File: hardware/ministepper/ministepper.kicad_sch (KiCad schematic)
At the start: 13 parts, among them J2 Conn_ARM_SWD_TagConnect_TC203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, U1 STM32G071G8U6, U4 SIT3088EEUA

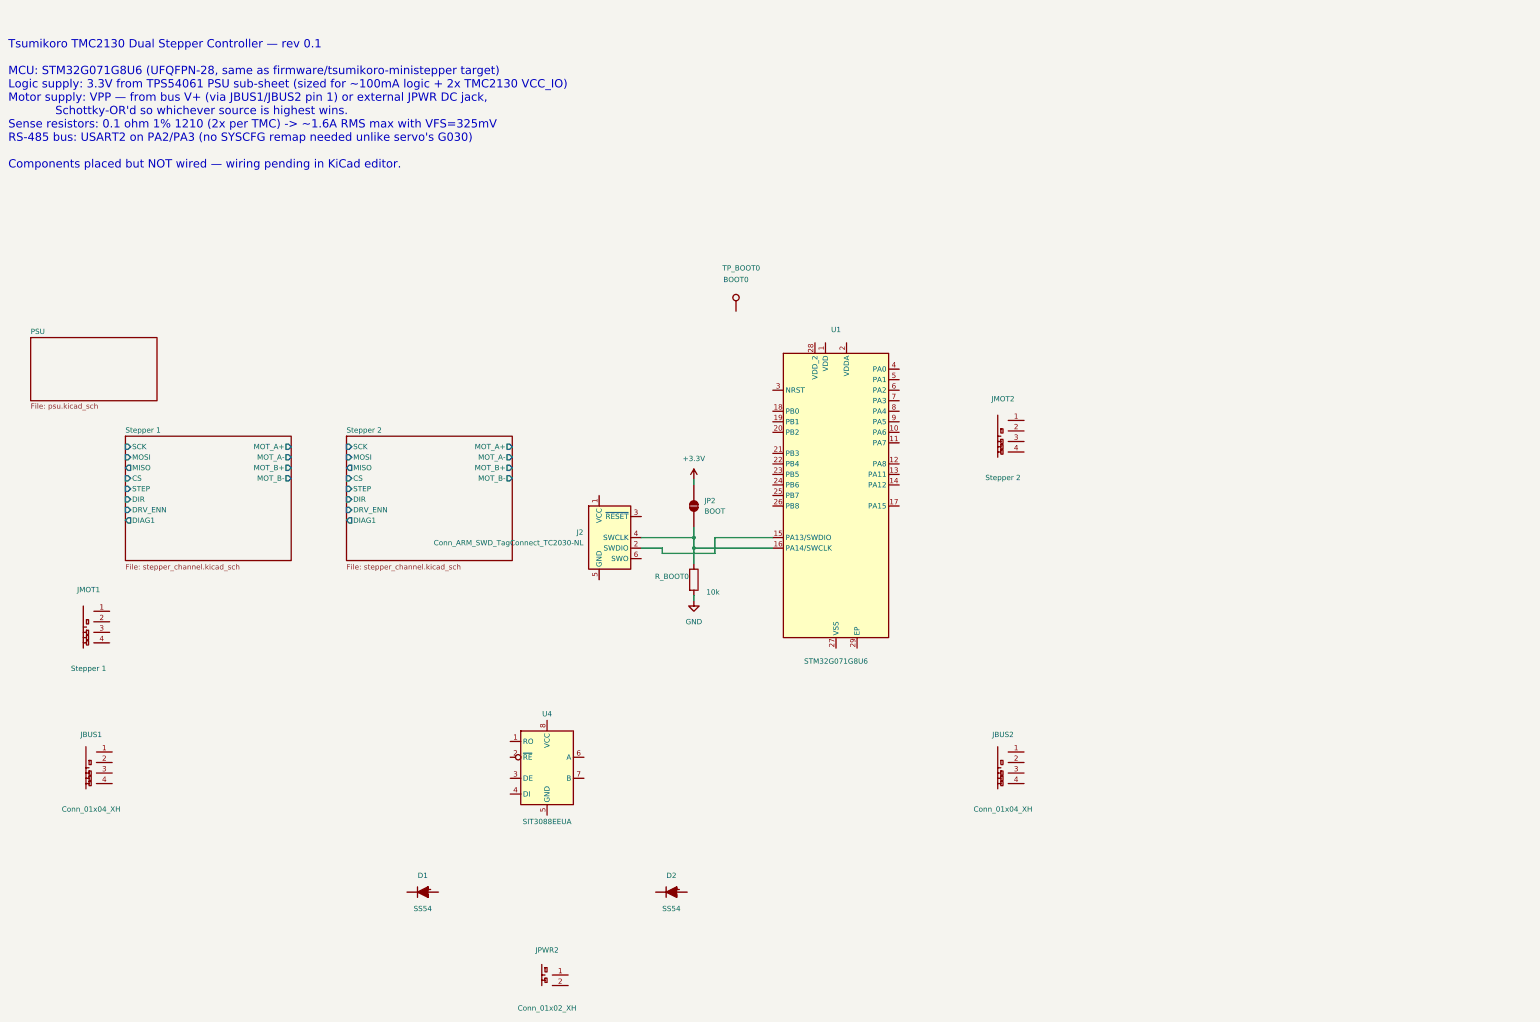
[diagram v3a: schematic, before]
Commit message: hw+fw: fix STM32G071G8U6 UFQFPN28 symbol + pin map
The tsumikoro:STM32G071G8U6 symbol had a fabricated pin map that
didn't match ST DS12232 Figure 9 — VDD/VDDA were split onto pins 1/2
(they're actually fused on pin 3 on this package), NRST was assigned
to pin 3 (it's on pin 5), pin 28 was labelled VDD_2 (it's PB8), and
DIR2 was on PB2 (which is not bonded out on UFQFPN28).

Because the ministepper is not yet wired and firmware addresses GPIOs
by port name, no PCB damage resulted — but every pin number in docs,
firmware comments, and the symbol was off.

Rewritten against the datasheet:

- Symbol rebuilt with the real 29-pin UFQFPN28 layout (28 signal +
  EP), including PC14/PC15 on pins 1/2 and PC6 on pin 17.
- DIR2 reassigned from phantom PB2 to PC6 (pin 17).
- GPIOC clock enabled in firmware for PC6.
- CLAUDE.md and ministepper/docs/README.md pin tables rewritten.
- docs/README now calls out required MCU decoupling (100 nF + 4.7 µF
  bulk + NRST filter) that was implicitly missing when docs assumed
  two separate VDD pins.

Co-Authored-By: Claude Opus 4.6 (1M context) <noreply@anthropic.com>
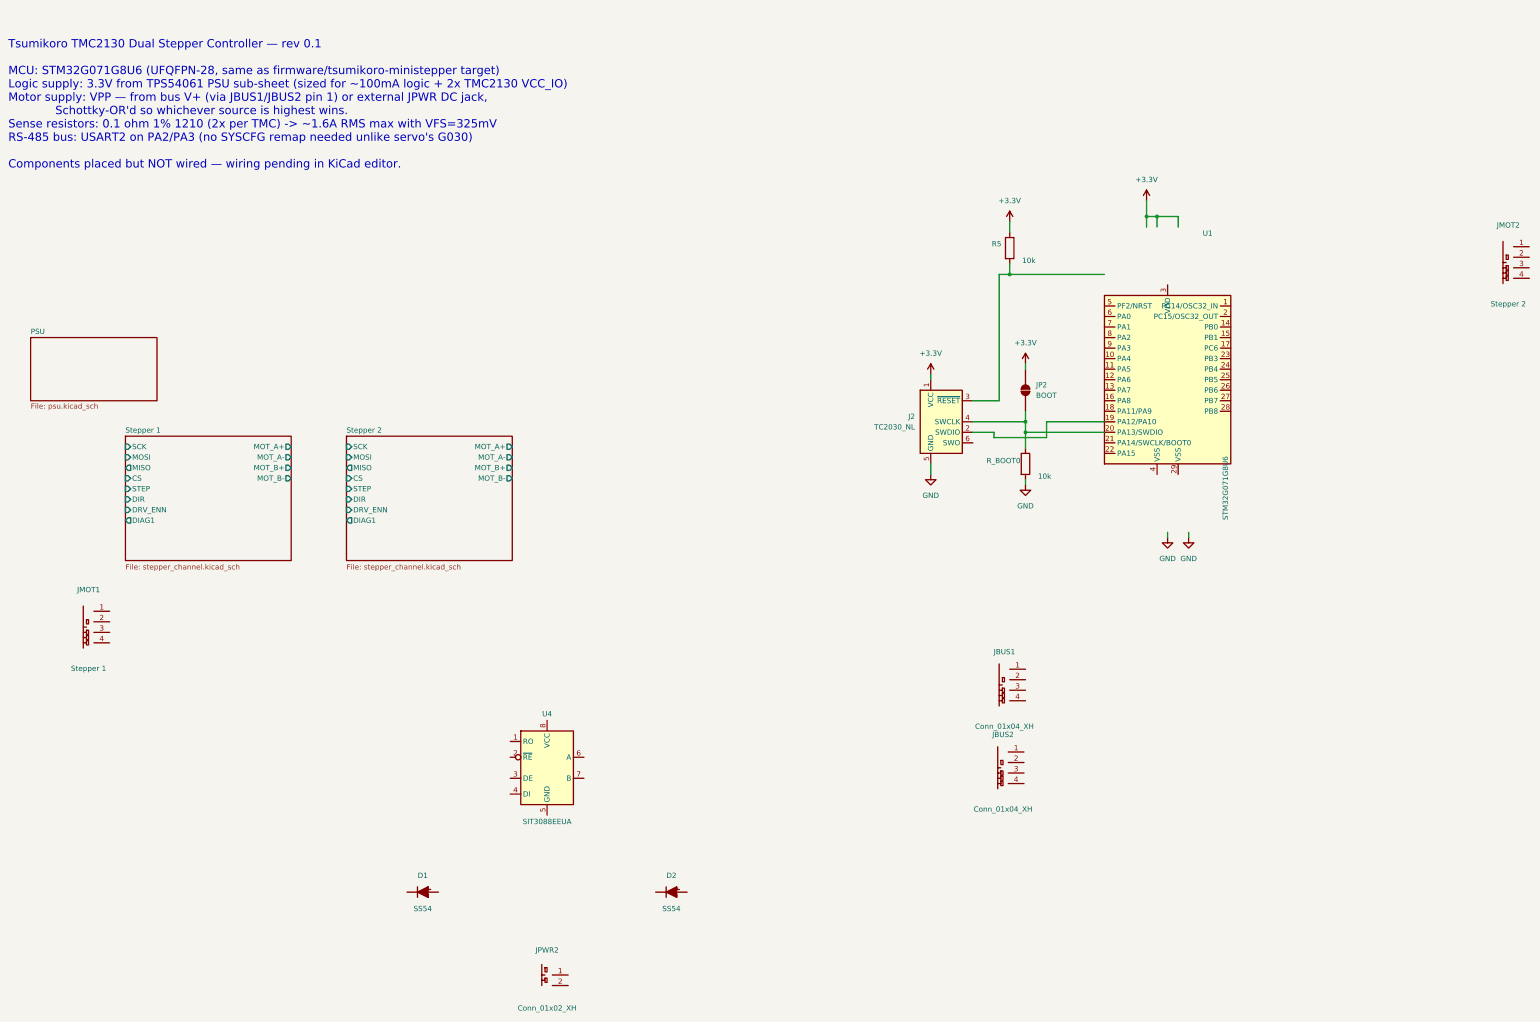
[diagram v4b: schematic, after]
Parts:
- removed TP_BOOT0: BOOT0, TestPoint:TestPoint_Pad_1.0x1.0mm, symbol Connector:TestPoint
- added R5: 10k, Resistor_SMD:R_0402_1005Metric, symbol Device:R
- J2: value Conn_ARM_SWD_TagConnect_TC2030-NL -> TC2030_NL
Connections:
- net +3.3V: now also J2.1 (VCC), R5.1
- net GND: now also J2.5 (GND)
- net at J2.2 (SWDIO): now also U1.19 (PA12/PA10); no longer U1.15 (PA13/SWDIO)
- net at J2.3 (~{RESET}): now also R5.2
- net at J2.4 (SWCLK), JP2.1 (A), R_BOOT0.1: now also U1.20 (PA13/SWDIO); no longer U1.16 (PA14/SWCLK)
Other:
- moved on the sheet: J2, JBUS1, JMOT2, JP2, R_BOOT0, U1

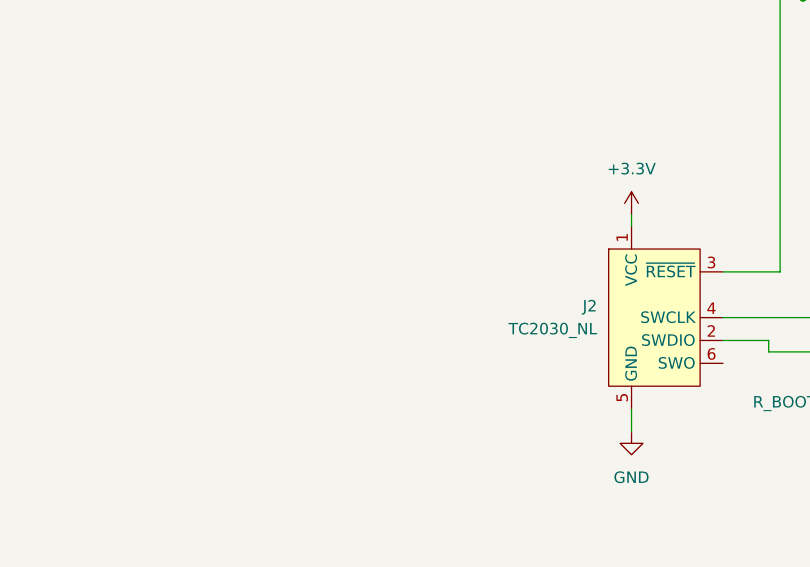
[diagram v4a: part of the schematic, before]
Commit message: hw/ministepper: add MCU decoupling + NRST filter caps
Rev 0.1 root schematic had zero MCU support caps on the STM32G071 —
all existing caps were PSU sub-sheet or TMC2130 sub-sheet parts. Per
ST AN2867 / G071 datasheet hardware design recommendations:

- C_MCU_VDD (100 nF 0402 C307331, basic) — VDD/VDDA HF bypass at pin 3.
- C_MCU_BULK (4.7 uF 0603 C19666 Samsung, basic) — bulk decoupling
  close to the VDD pin.
- C_NRST (100 nF 0402 C307331, basic) — noise filter on NRST pin 5.

Also embedded Device:C in the root schematic's lib_symbols block.
Without that embedding, any root-level capacitor would silently fail
BOM export — KiCad drops symbols whose lib_id isn't cached in the
schematic. Only Device:R had been embedded previously.

Co-Authored-By: Claude Opus 4.6 (1M context) <noreply@anthropic.com>
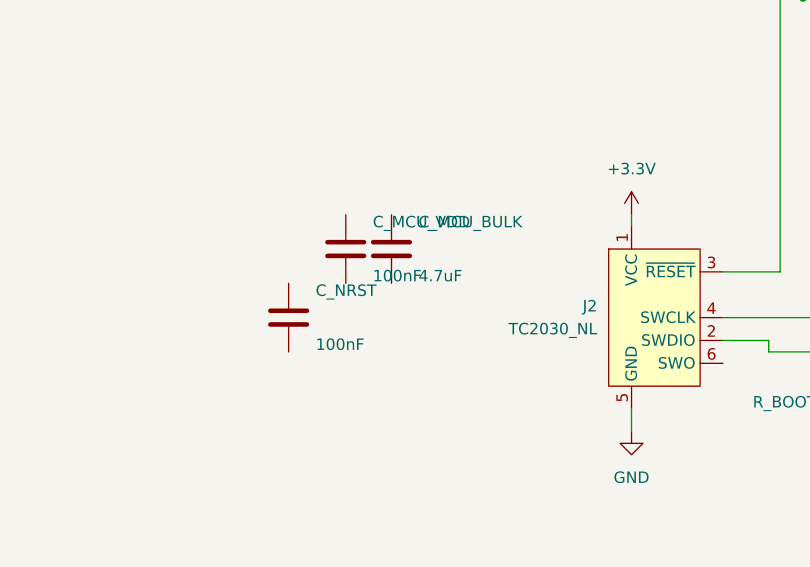
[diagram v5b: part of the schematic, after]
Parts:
- added C_MCU_BULK: 4.7uF, Capacitor_SMD:C_0603_1608Metric, symbol Device:C
- added C_MCU_VDD, C_NRST: 100nF, Capacitor_SMD:C_0402_1005Metric, symbol Device:C

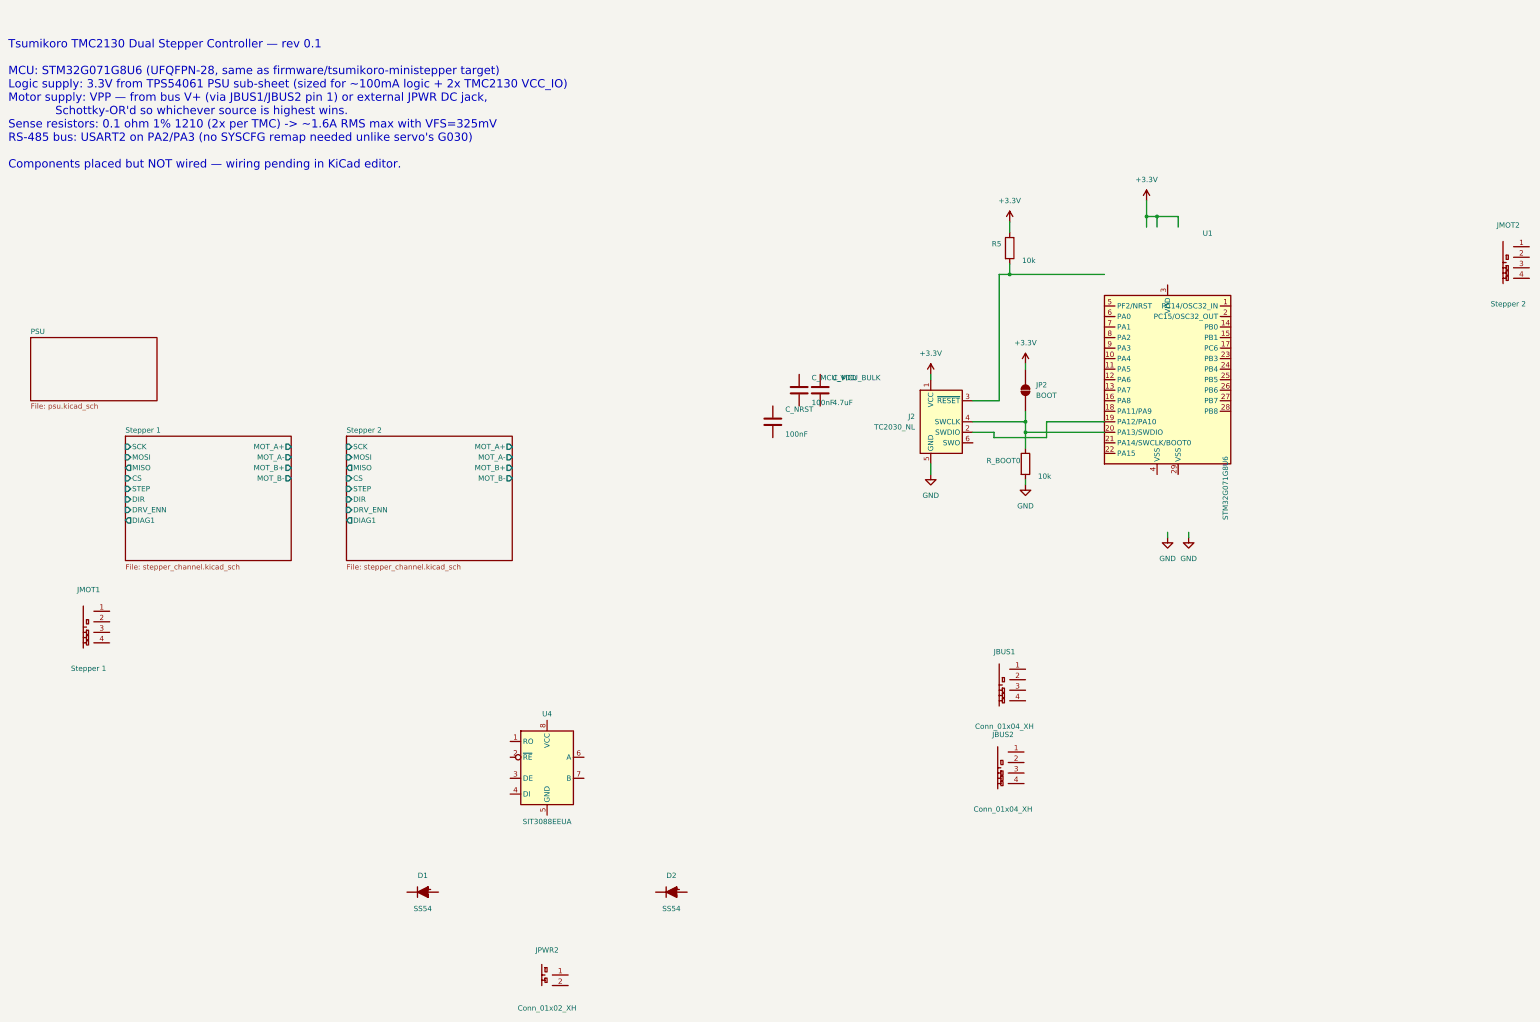
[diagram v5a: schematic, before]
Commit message: hw/ministepper: swap MCU to STM32G0B1KBU6 (USB) + add USB-C connector
Replace the STM32G071G8U6 (UFQFPN-28, no USB) with STM32G0B1KBU6
(UFQFPN-32, USB 2.0 FS, 128KB flash, 144KB RAM). This frees PA11/PA12
for USB D−/D+ by giving PA9/PA10 as separate pins.

Hardware changes:
- New UFQFPN-32 5x5mm footprint + STEP model (from EasyEDA C5159549)
- New tsumikoro:STM32G0B1KBU6 symbol with 32-pin + EP layout
- J_USB: GCT USB4105-xx-A 16-pin USB-C receptacle (C2927039, same as
  bridge board) with R_CC1/R_CC2 5.1k pull-downs for device/sink
- DRV_ENN moved PA11 → PB2 (pin 17)
- TMC2_CS moved PA12 → PA9 (pin 19)
- PA11 (pin 22) = USB D−, PA12 (pin 23) = USB D+
- No external crystal needed (HSI48 + CRS from USB SOF)

Firmware:
- PIN_DRV_ENN: GPIOA/11 → GPIOB/2
- PIN_TMC2_CS: GPIOA/12 → GPIOA/9
- Target header updated to rev 0.2 / UFQFPN-32

Docs: CLAUDE.md and ministepper/docs/README.md pin maps rewritten
for the 32-pin layout.

Co-Authored-By: Claude Opus 4.6 (1M context) <noreply@anthropic.com>
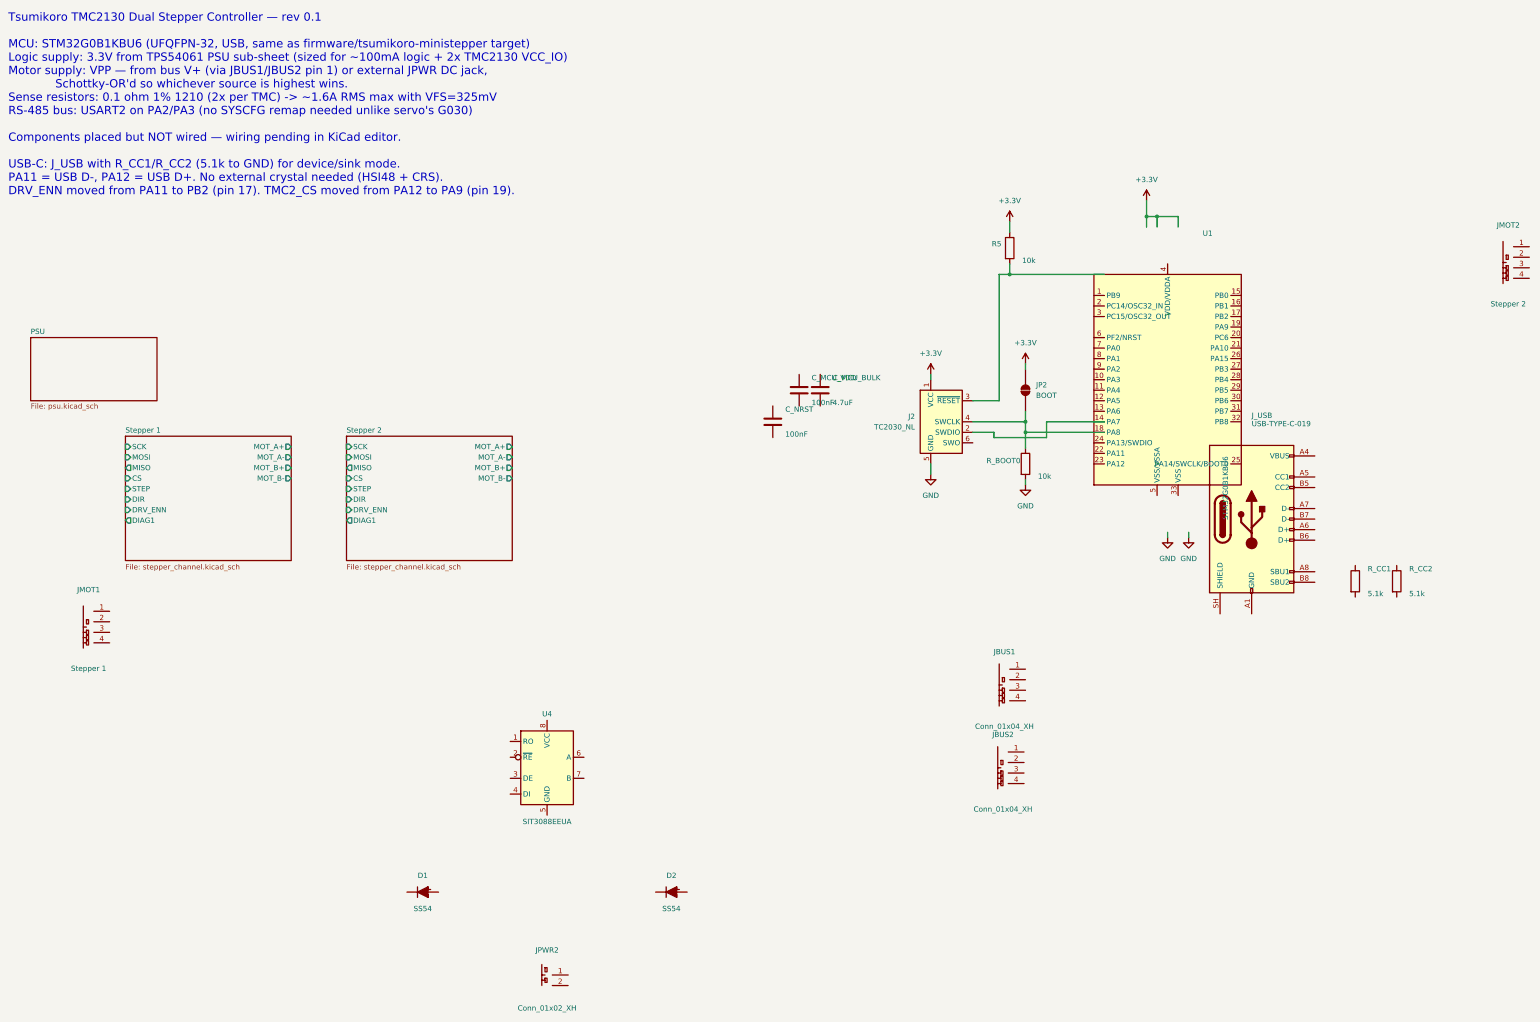
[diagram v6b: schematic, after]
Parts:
- added J_USB: USB-TYPE-C-019, Connector_USB:USB_C_Receptacle_GCT_USB4105-xx-A_16P_TopMnt_Horizontal, symbol Connector:USB_C_Receptacle_USB2.0_16P
- added R_CC1, R_CC2: 5.1k, Resistor_SMD:R_0402_1005Metric, symbol Device:R
- U1: value STM32G071G8U6 -> STM32G0B1KBU6; footprint tsumikoro:UFQFPN-28 -> tsumikoro:UFQFPN-32; symbol tsumikoro:STM32G071G8U6 -> tsumikoro:STM32G0B1KBU6; LCSC C724080 -> C5159549; MPN STM32G071G8U6 -> STM32G0B1KBU6
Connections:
- net at J2.2 (SWDIO): no longer U1.19 (PA12/PA10)
- net at J2.4 (SWCLK), JP2.1 (A), R_BOOT0.1: no longer U1.20 (PA13/SWDIO)
- new net: J_USB.A1 (GND), J_USB.A12 (GND), J_USB.B1 (GND), J_USB.B12 (GND)
- new net: J_USB.A4 (VBUS), J_USB.A9 (VBUS), J_USB.B4 (VBUS), J_USB.B9 (VBUS)
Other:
- note added: "Tsumikoro TMC2130 Dual Stepper Controller — rev 0.1 MCU: STM32G0B1KBU6 (UFQFPN-32, USB, same as firmware/tsumikoro-ministepper target) Logic supply: 3.3V from TPS54061 PSU sub-sheet (sized for ~100mA logic + 2x TMC2130 VCC_IO) Motor supply: VPP — from bus V+ (via JBUS1/JBUS2 pin 1) or external JPWR DC jack, Schottky-OR'd so whichever source is highest wins. Sense resistors: 0.1 ohm 1% 1210 (2x pe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"
- note removed: "Tsumikoro TMC2130 Dual Stepper Controller — rev 0.1 MCU: STM32G071G8U6 (UFQFPN-28, same as firmware/tsumikoro-ministepper target) Logic supply: 3.3V from TPS54061 PSU sub-sheet (sized for ~100mA logic + 2x TMC2130 VCC_IO) Motor supply: VPP — from bus V+ (via JBUS1/JBUS2 pin 1) or external JPWR DC jack, Schottky-OR'd so whichever source is highest wins. Sense resistors: 0.1 ohm 1% 1210 (2x per TMC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"
